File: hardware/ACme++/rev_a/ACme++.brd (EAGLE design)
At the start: 72.6 x 47.1 mm, 96 parts, among them J2 TC2030-CTX-NL, J3 WIRE_HOLE-14AWG, J4 WIRE_HOLE-14AWG, K1 S216S01F, Q1 STGD5NB120SZT4, Q2 FDV301N, U1 CC2538, U2 DS2411, U3 FM25LBTDFN-8, U4 ADE7753, U5 TXB0104RGY, U6 SR086SG-G, U7 TDA3664AT, X1 EPSON-FA-128, X2 FC-12M32.7680KA-A3, X3 ECS-35-17-5PX-TR

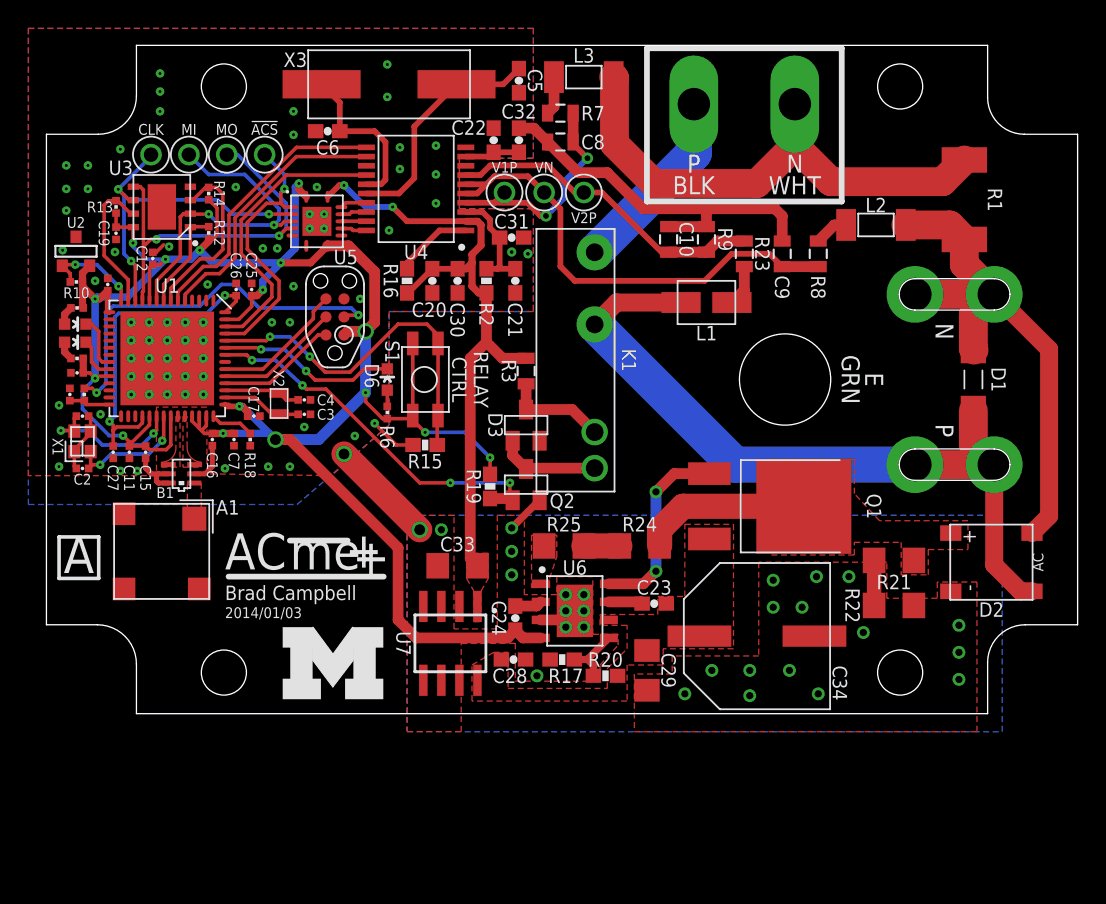
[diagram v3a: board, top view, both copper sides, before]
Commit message: moved phase trace
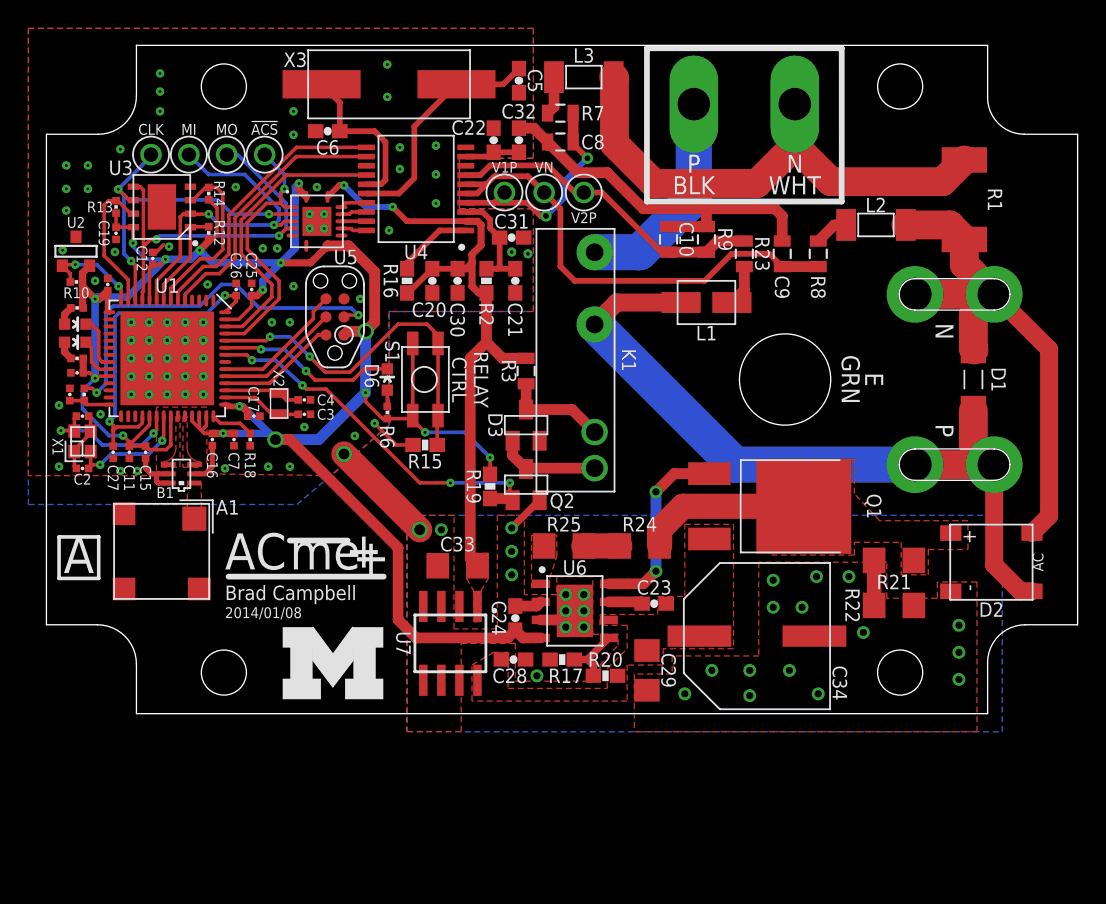
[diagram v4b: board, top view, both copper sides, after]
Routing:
- net LOAD_PHASE: track 13.3 -> 15.2 mm
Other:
- board text added: "2014/01/08"
- board text removed: "2014/01/03"
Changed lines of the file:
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@@
 <text x="22.86" y="11.049" size="2.54" layer="21" font="fixed" align="center">+</text>
 <text x="12.573" y="8.001" size="1.016" layer="21" font="vector" ratio="13">Brad Campbell</text>
-<text x="12.573" y="6.731" size="0.762" layer="21" font="vector" ratio="12">2014/01/03</text>
+<text x="12.573" y="6.731" size="0.762" layer="21" font="vector" ratio="12">2014/01/08</text>
 <text x="2.286" y="11.176" size="2.54" layer="21" font="fixed" ratio="12" align="center">A</text>
 <wire x1="0.889" y1="12.446" x2="0.889" y2="9.525" width="0.254" layer="21"/>
@@
 <text x="63.881" y="19.939" size="1.27" layer="21" font="vector" ratio="12" rot="SR270" align="top-center">P</text>
 <polygon width="0" layer="30" spacing="0.254">
-<vertex x="38.1" y="33.02"/>
-<vertex x="39.116" y="32.004"/>
-<vertex x="46.355" y="39.243"/>
+<vertex x="38.608" y="31.623"/>
+<vertex x="42.037" y="31.623"/>
+<vertex x="46.355" y="35.941"/>
 <vertex x="46.355" y="43.18"/>
 <vertex x="44.831" y="43.18"/>
-<vertex x="44.831" y="39.751"/>
+<vertex x="44.831" y="36.703"/>
+<vertex x="41.529" y="33.401"/>
+<vertex x="38.608" y="33.401"/>
 </polygon>
 <polygon width="0" layer="30" spacing="0.254">
@@
 <vertex x="44.831" y="43.18"/>
 <vertex x="46.355" y="43.18"/>
-<vertex x="46.355" y="39.243"/>
-<vertex x="39.116" y="32.004"/>
-<vertex x="38.1" y="33.02"/>
-<vertex x="44.831" y="39.751"/>
+<vertex x="46.355" y="35.941"/>
+<vertex x="42.037" y="31.623"/>
+<vertex x="38.608" y="31.623"/>
+<vertex x="38.608" y="33.401"/>
+<vertex x="41.529" y="33.401"/>
+<vertex x="44.831" y="36.703"/>
 </polygon>
 <text x="7.366" y="40.767" size="0.762" layer="21" font="vector" ratio="12" align="bottom-center">CLK</text>
@@
 <contactref element="J3" pad="P$1"/>
 <contactref element="K1" pad="1"/>
-<wire x1="38.608" y1="32.494" x2="45.593" y2="39.479" width="2.54" layer="16"/>
-<wire x1="45.593" y1="39.479" x2="45.593" y2="42.926" width="2.54" layer="16"/>
+<wire x1="38.608" y1="32.494" x2="41.765" y2="32.494" width="2.54" layer="16"/>
+<wire x1="41.765" y1="32.494" x2="45.593" y2="36.322" width="2.54" layer="16"/>
+<wire x1="45.593" y1="36.322" x2="45.593" y2="42.926" width="2.54" layer="16"/>
 </signal>
 <signal name="N$16">
